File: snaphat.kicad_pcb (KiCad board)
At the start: 2 copper layers, 100 x 65.1 mm, 111 parts, among them J1 Conn_01x08_S8B-PH-K-S(LF)(SN), J2 Conn_02x20_2214SM-40G-75-PCR, J3 Conn_01x02_B2B-PH-K-S(LF)(SN), J4 USB_C_USB4125-GF-A-0190, J5 Conn_01x03_MC34747, Q1 Q_BC817-25, Q2 Q_NTR4003NT1G, Q3 Q_NTR4003NT1G, SW1 SW_B3FS-1050, SW2 SW_B3FS-1050, SW3 SW_B3FS-1050, SW4 SW_B3FS-1050, SW5 SW_B3FS-1050, SW6 SW_B3FS-1050, SW7 SW_B3FS-1050, SW8 SW_B3F-3150, U1 INA219BIDR, U2 MPQ3414BGJ-5-AEC1-P, U3 MCP73871T-2CCI/ML, U4 1825232-1, U5 AP9101CAK6-ABTRG1, U6 LIS2DW12TR

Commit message: Start updating PCB, library fixes
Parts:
- removed C4: 10u, library:C_0805_2012Metric
- removed C5: 1u, library:C_0805_2012Metric
- removed Q3: Q_NTR4003NT1G, library:SOT-23
- removed R17, R19: 0R, library:R_0402_1005Metric
- removed R2: 10k, library:R_0402_1005Metric
- removed REF** (x8): , library:TestPoint_Ornament
- removed REF** (x4): MountingHole_2.7mm, library:MountingHole_2.7mm
- added C10: 10u, library:C_0805_2012Metric, F.Cu at (239.9, 114.5)
- added D6: SL04-E3-08, library:DO-219AB, F.Cu at (231.7, 111.4)
- added D7: SL04-E3-08, library:DO-219AB, F.Cu at (216.7, 114.6)
- added D8: D_SMBJ5.0A, library:D_SMB, F.Cu at (225.4, 130.5)
- added H34: 9774020951R, library:Mounting_Wuerth_WA-SMST-2.7mm_H2mm_9774020951, F.Cu at (175.5, 21.7)
- added H35: 9774020951R, library:Mounting_Wuerth_WA-SMST-2.7mm_H2mm_9774020951, F.Cu at (175.5, 29.2)
- added H36: 9774020951R, library:Mounting_Wuerth_WA-SMST-2.7mm_H2mm_9774020951, F.Cu at (175.5, 36.8)
- added H37: 9774020951R, library:Mounting_Wuerth_WA-SMST-2.7mm_H2mm_9774020951, F.Cu at (175.5, 44.3)
- added J10: P70-6000045R, library:HARWIN_P70-6000045R, F.Cu at (190.9, 25.5)
- added J11: P70-6000045R, library:HARWIN_P70-6000045R, F.Cu at (190.9, 28.6)
- added J12: P70-6000045R, library:HARWIN_P70-6000045R, F.Cu at (190.9, 31.6)
- added J6: Conn_01x04_SFV4R-3STBE1HLF/C, library:AMPHENOL_SFV4R-3STBE1HLF, B.Cu at (193.1, 121.8)
- added J7: Conn_01x04_SFV4R-3STBE1HLF/C, library:AMPHENOL_SFV4R-3STBE1HLF, B.Cu at (175.5, 21.4)
- added J8: P70-6000045R, library:HARWIN_P70-6000045R, F.Cu at (190.9, 19.4)
- added J9: P70-6000045R, library:HARWIN_P70-6000045R, F.Cu at (190.9, 22.5)
- added R28: 330R, library:R_0402_1005Metric, F.Cu at (188.0, 38.9)
- added SW9: 1825232-1, library:1825232-1, B.Cu at (244.2, 113.4)
- C3: value 22u -> 2u2
- D2: value 0805 G LED -> 0805 B LED
- D4: value 0805 B LED -> 0805 R LED
- H15: value 803040 -> 10304
- H26, H27, H28, H29: value 9774030633R -> 9774030151R; footprint library:Mounting_Wuerth_WA-SMSI-M1.6_H3mm_9774030633 -> library:Mounting_Wuerth_WA-SMSI-M2.5_H3mm_9774030151R
- H30, H31, H32: value 970110151 -> 9774100151R; footprint library:970110151 -> library:Mounting_Wuerth_WA-SMSI-M2.5_H10mm_9774100151R
- J4: value USB_C_USB4125-GF-A-0190 -> USB_C_USB4930-00-A; footprint library:USB_C_Receptacle_GCT_USB4125-xx-x-0190_6P_TopMnt_Horizontal -> library:USB_C_Receptacle_GCT_USB4105-xx-A_16P_TopMnt_Horizontal
- L1: value L_SRP3212A-R68M -> L_LQH44PH100MPRL; footprint library:L_1210_3225Metric -> library:L_LPH44PH
- Q2: value Q_NTR4003NT1G -> Q_FDC6561AN; footprint library:SOT-23 -> library:SSOT-6
- R10: value 150R -> 47R
- R14: value 10k -> 2k7
- R6: value 10k -> 100k
- R7: value 10k -> 33k
- R9: value 150R -> 100R
- U2: value MPQ3414BGJ-5-AEC1-P -> MIC2250-1YD5-TR; footprint library:TSOT-23-8 -> library:TSOT-23-5
- U4: value 1825232-1 -> TPD2EUSB30DRTR; footprint library:1825232-1 -> library:Texas_DRT-3
- moved U4 28.4 mm to (216.2, 117.2), turned to 0 degrees
- moved TP11 21.6 mm to (257.3, 103.9)
- moved C2 13.3 mm to (214.1, 129.4)
- moved C15 12.6 mm to (211.5, 129.3)
- moved R4 9.79 mm to (219.2, 129.8), turned to 90 degrees
- moved R5 9.17 mm to (217.9, 129.8), turned to 90 degrees
- moved L1 6.25 mm to (235.4, 109.4), turned to 180 degrees
- moved C13 5.80 mm to (229.9, 110.3), turned to 90 degrees
- moved C3 5.78 mm to (228.2, 110.8), turned to -90 degrees
- moved TP8 4.62 mm to (240.1, 110.4), turned to 180 degrees
- moved R20 4.38 mm to (237.7, 122.6), turned to 180 degrees
- moved R23 3.25 mm to (239.7, 120.8)
- moved C14 3.10 mm to (238.2, 113.7), turned to 90 degrees
- moved R13 2.57 mm to (219.9, 111.4), turned to -90 degrees
- moved C21 2.11 mm to (221.0, 111.4)
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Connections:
- net +BATT renamed VBAT
- net ACCEL_INT1 renamed /ACCEL_INT1
- net ACCEL_INT2 renamed /ACCEL_INT2
- net BTN_BACK renamed /BTN_B
- net BTN_MENU renamed /BTN_MENU
- net BTN_OK renamed /BTN_A
- net CHARGING_STAT renamed /Power supply/CHRG_DONE_STAT
- net I2C_SCL renamed /I2C_SCL
- net I2C_SDA renamed /I2C_SDA
- net Net-(J3-Pin_1) renamed /Power supply/BATTERY_P
- net PROG1 renamed /Power supply/PROG1
- net PROG2 renamed /Power supply/PROG2
- net TIMER_EN renamed Net-(U3-~{TE})
- C15 pad 2: VBUS -> /USBC_VBUS_IN
- C17 pad 2: Net-(C17-Pad2) -> /Power supply/VOUT
- C2 pad 1: VBUS -> /USBC_VBUS_IN
- D3 pad 2: VBUS -> /LOW_BATTERY
- J1 pad 2: GND -> +5V
- J1 pad 5: DISPLAY_SPI_CS -> +5V
- J1 pad 6: DISPLAY_DC -> +5V
- J1 pad 7: DISPLAY_RST -> +5V
- J1 pad 8: DISPLAY_BL -> +5V
- J2 pad 10: RPI_UART_RX -> GND
- J2 pad 12: BUZZER_SIGNAL -> GND
- J2 pad 18: DISPLAY_RST -> GND
- J2 pad 19: DISPLAY_SPI_MOSI -> /DISPLAY_MOSI
- J2 pad 22: DISPLAY_DC -> GND
- J2 pad 23: DISPLAY_SPI_SCLK -> /DISPLAY_SPI_SCLK
- J2 pad 24: DISPLAY_SPI_CS -> GND
- J2 pad 27: unconnected-(J2-Pin_27-Pad27) -> /BTN_D
- J2 pad 29: BTN_D -> /BTN_L
- J2 pad 31: BTN_L -> /BTN_R
- J2 pad 32: DISPLAY_BL -> GND
- J2 pad 33: BTN_R -> /BTN_U
- J2 pad 35: BTN_U -> /LOW_BATTERY
- J2 pad 37: BTN_SHUTTER -> /BTN_SHUTTER
- J2 pad 8: RPI_UART_TX -> GND
- J4 pad A9: VBUS -> /USBC_VBUS_IN
- J4 pad B9: VBUS -> /USBC_VBUS_IN
- J5 pad 1: RPI_UART_RX -> GND
- J5 pad 2: RPI_UART_TX -> GND
- L1 pad 2: Net-(U2-SW) -> Net-(D6-A)
- Q1 pad 1: Net-(Q1-C) -> Net-(Q1-B)
- Q1 pad 2: Net-(Q1-B) -> GND
- Q1 pad 3: GND -> Net-(BZ1--)
- Q2 pad 1: Net-(Q2-D) -> Net-(U5-DO)
- Q2 pad 2: Net-(Q2-G) -> GND
- Q2 pad 3: GNDS -> Net-(U5-CO)
- R1 pad 1: BUZZER_SIGNAL -> GND
- R10 pad 1: LBO_STAT -> GND
- R14 pad 1: PROG3 -> GND
- R14 pad 2: GND -> /Power supply/PROG3
- R18 pad 1: PS_SELECT -> VBUS
- R18 pad 2: VBUS -> Net-(U3-SEL)
- R27 pad 1: Net-(BZ1--) -> /GND_EXT
- R27 pad 2: Net-(Q1-C) -> /OTG_EXT
- R4 pad 1: Net-(J4-CC2) -> GND
- R4 pad 2: GND -> Net-(J4-CC1)
- R5 pad 1: Net-(J4-CC1) -> GND
- R5 pad 2: GND -> Net-(J4-CC2)
- R6 pad 1: VSYS -> +5V
- R6 pad 2: Net-(U2-MODE) -> Net-(U2-FB)
- R7 pad 1: VSYS -> Net-(U2-FB)
- R7 pad 2: Net-(U2-EN) -> GND
- R8 pad 1: POWER_GOOD -> /Power supply/CHRG_STAT
- SW4 pad 1: BTN_U -> /BTN_U
- SW4 pad 2: BTN_U -> /BTN_U
- SW5 pad 1: BTN_L -> /BTN_L
- SW5 pad 2: BTN_L -> /BTN_L
- SW6 pad 1: BTN_R -> /BTN_R
- SW6 pad 2: BTN_R -> /BTN_R
- SW7 pad 1: BTN_D -> /BTN_D
- SW7 pad 2: BTN_D -> /BTN_D
- SW8 pad 1: BTN_SHUTTER -> /BTN_SHUTTER
- SW8 pad 2: BTN_SHUTTER -> GND
- U2 pad 1: VSYS -> Net-(D6-A)
- U2 pad 2: +5V -> GND
- U2 pad 3: Net-(U2-SW) -> Net-(U2-FB)
- U2 pad 4: GND -> VSYS
- U2 pad 5: GND -> VSYS
- U3 pad 1: Net-(C17-Pad2) -> /Power supply/VOUT
- U3 pad 12: PROG3 -> /Power supply/PROG3
- U3 pad 20: Net-(C17-Pad2) -> /Power supply/VOUT
- U3 pad 3: PS_SELECT -> Net-(U3-SEL)
- U3 pad 6: POWER_GOOD -> unconnected-(U3-~{PG}-Pad6)
- U3 pad 8: LBO_STAT -> /Power supply/CHRG_STAT
- U4 pad 1: Net-(C17-Pad2) -> /USBC_DATA_P
- U4 pad 2: VSYS -> /USBC_DATA_N
- U4 pad 3: unconnected-(U4-Pad3) -> GND
- U5 pad 1: Net-(Q2-G) -> Net-(U5-DO)
- U5 pad 3: Net-(Q3-G) -> Net-(U5-CO)
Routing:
- net +5V: track 113.5 -> 304.9 mm, vias 3 -> 11
- net VBUS: track 112.9 -> 3.99 mm, vias 5 -> 0
- net BTN_R: track 69.7 -> 0.00 mm, vias 1 -> 0
- net /BTN_R: track 0.00 -> 68.3 mm, vias 0 -> 1
- net /LOW_BATTERY: track 0.00 -> 64.3 mm, vias 0 -> 1
- net BTN_D: track 62.8 -> 0.00 mm, vias 1 -> 0
- net BTN_U: track 62.1 -> 0.00 mm, vias 1 -> 0
- net /BTN_D: track 0.00 -> 61.1 mm, vias 0 -> 1
- net /BTN_U: track 0.00 -> 59.1 mm, vias 0 -> 1
- net GND: track 42.0 -> 97.6 mm, vias 22 -> 1
- net BTN_SHUTTER: track 53.8 -> 0.00 mm
- net BTN_L: track 52.5 -> 0.00 mm, vias 1 -> 0
- net /BTN_L: track 0.00 -> 51.9 mm, vias 0 -> 1
- net LBO_STAT: track 51.2 -> 0.00 mm, vias 1 -> 0
- net DISPLAY_RST: track 50.6 -> 0.00 mm
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- added copper zone on B.Cu, net /Power supply/VOUT
- added copper zone on F.Cu, net Net-(D6-A)
- added copper zone on B.Cu, net Net-(Q2-Pad4)
- removed copper zone on B.Cu, net Net-(C17-Pad2)
- removed copper zone on F.Cu, net Net-(U2-SW)

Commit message: Rerouted power and USB
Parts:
- removed U4: TPD2EUSB30DRTR, library:Texas_DRT-3
- added C22: 100n, library:C_0402_1005Metric, B.Cu at (212.8, 120.0)
- added D9: SP1004U-ULC-04UTG, library:SP1004UULC04UTG, B.Cu at (215.7, 119.0)
- added REF**: MountingHole_2.7mm, MountingHole:MountingHole_2.7mm, F.Cu at (243.7, 125.5)
- C15, C2, D7, R11, R4, R5, TP6: moved to B.Cu
- D8: footprint library:D_SMB -> library:SOD-123FL
- moved TP11 23.1 mm to (234.8, 109.4), turned to -90 degrees
- moved TP6 15.8 mm to (228.3, 118.4), turned to 90 degrees
- moved C2 13.2 mm to (222.4, 119.2)
- moved R5 13.1 mm to (214.1, 117.3), turned to 0 degrees
- moved R4 12.6 mm to (217.4, 117.3), turned to 180 degrees
- moved C15 12.3 mm to (219.6, 120.0)
- moved D8 10.3 mm to (216.2, 126.1), turned to -90 degrees
- moved R9 8.07 mm to (222.3, 122.4)
- moved R11 6.71 mm to (229.0, 109.1), turned to 180 degrees
- moved R8 5.46 mm to (223.3, 122.4)
- moved D7 4.00 mm to (220.2, 116.6), turned to -90 degrees
- moved R22 3.74 mm to (239.0, 125.7)
- moved R3 3.20 mm to (235.3, 113.5)
- moved J5 3.13 mm to (170.4, 118.1)
- moved U1 3.04 mm to (234.0, 119.5)
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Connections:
- J1 pad 2: +5V -> GND
- J1 pad 3: DISPLAY_SPI_MOSI -> /DISPLAY_MOSI
- J1 pad 4: DISPLAY_SPI_SCLK -> /DISPLAY_SPI_SCLK
- J1 pad 5: +5V -> GND
- J1 pad 6: +5V -> GND
- J1 pad 7: +5V -> GND
- J1 pad 8: +5V -> GND
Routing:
- net GND: track 97.6 -> 223.6 mm, vias 1 -> 14
- net +5V: track 304.9 -> 183.9 mm, vias 11 -> 7
- net VBUS: track 3.99 -> 55.9 mm, vias 0 -> 7
- net DISPLAY_SPI_MOSI: track 50.3 -> 0.00 mm
- net DISPLAY_SPI_SCLK: track 42.0 -> 0.00 mm
- net /DISPLAY_MOSI: track 0.00 -> 40.6 mm
- net /I2C_SCL: track 61.9 -> 101.6 mm
- net +3.3V: track 147.3 -> 182.3 mm, vias 6 -> 8
- net /DISPLAY_SPI_SCLK: track 0.00 -> 32.5 mm
- net /I2C_SDA: track 72.0 -> 101.5 mm
- net /BTN_B: track 21.3 -> 32.5 mm
- net /Power supply/VOUT: track 48.2 -> 37.9 mm
- net Net-(D2-K): track 1.55 -> 10.7 mm
- net /USBC_VBUS_IN: track 0.00 -> 8.52 mm, vias 0 -> 4
- net /BTN_MENU: track 23.0 -> 31.3 mm
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- added copper zone on B.Cu, net /USBC_VBUS_IN
- added copper zone on F.Cu, net /USBC_VBUS_IN
- removed copper zone on B.Cu, net Net-(Q2-Pad4)
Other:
- board size 100 x 65.1 mm -> 100 x 68.1 mm

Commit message: Fix RPi connector on schematic, route rest of signals
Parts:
- removed REF**: MountingHole_2.7mm, MountingHole:MountingHole_2.7mm
- moved R27 78.6 mm to (187.5, 43.4)
- moved R1 1.99 mm to (159.6, 110.5)
- moved R6 0.84 mm to (234.8, 116.3), turned to 180 degrees
- moved R7 0.71 mm to (234.8, 117.3), turned to 0 degrees
- moved Q1 0.08 mm to (158.2, 113.0), turned to 180 degrees
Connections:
- J1 pad 5: GND -> /DISPLAY_SPI_CS
- J1 pad 6: GND -> /DISPLAY_DC
- J1 pad 7: GND -> /DISPLAY_RST
- J1 pad 8: GND -> /DISPLAY_BL
- J2 pad 10: GND -> /RPI_UART_RX
- J2 pad 12: GND -> /BUZZER_SIGNAL
- J2 pad 18: GND -> /DISPLAY_RST
- J2 pad 22: GND -> /DISPLAY_DC
- J2 pad 24: GND -> /DISPLAY_SPI_CS
- J2 pad 32: GND -> /DISPLAY_BL
- J2 pad 8: GND -> /RPI_UART_TX
- J5 pad 1: GND -> /RPI_UART_RX
- J5 pad 2: GND -> /RPI_UART_TX
- R1 pad 1: GND -> /BUZZER_SIGNAL
- R28 pad 1: GND -> /DISPLAY_BL
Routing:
- net GND: track 223.6 -> 92.6 mm, vias 14 -> 20
- net +5V: track 183.9 -> 121.8 mm, vias 7 -> 3
- net /DISPLAY_RST: track 0.00 -> 49.6 mm
- net /DISPLAY_BL: track 0.00 -> 44.1 mm
- net /DISPLAY_DC: track 0.00 -> 43.4 mm
- net /DISPLAY_SPI_CS: track 0.00 -> 39.3 mm
- net /BUZZER_SIGNAL: track 0.00 -> 24.1 mm
- net /RPI_UART_RX: track 0.00 -> 18.8 mm
- net /RPI_UART_TX: track 0.00 -> 15.1 mm
- net /DISPLAY_SPI_SCLK: track 32.5 -> 42.0 mm
- net /DISPLAY_MOSI: track 40.6 -> 49.8 mm
- net /BTN_B: track 32.5 -> 37.7 mm
- net Net-(BZ1--): track 6.79 -> 8.76 mm
- net /I2C_SCL: track 101.6 -> 102.7 mm
- net Net-(U1-VIN+): track 25.4 -> 24.5 mm
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
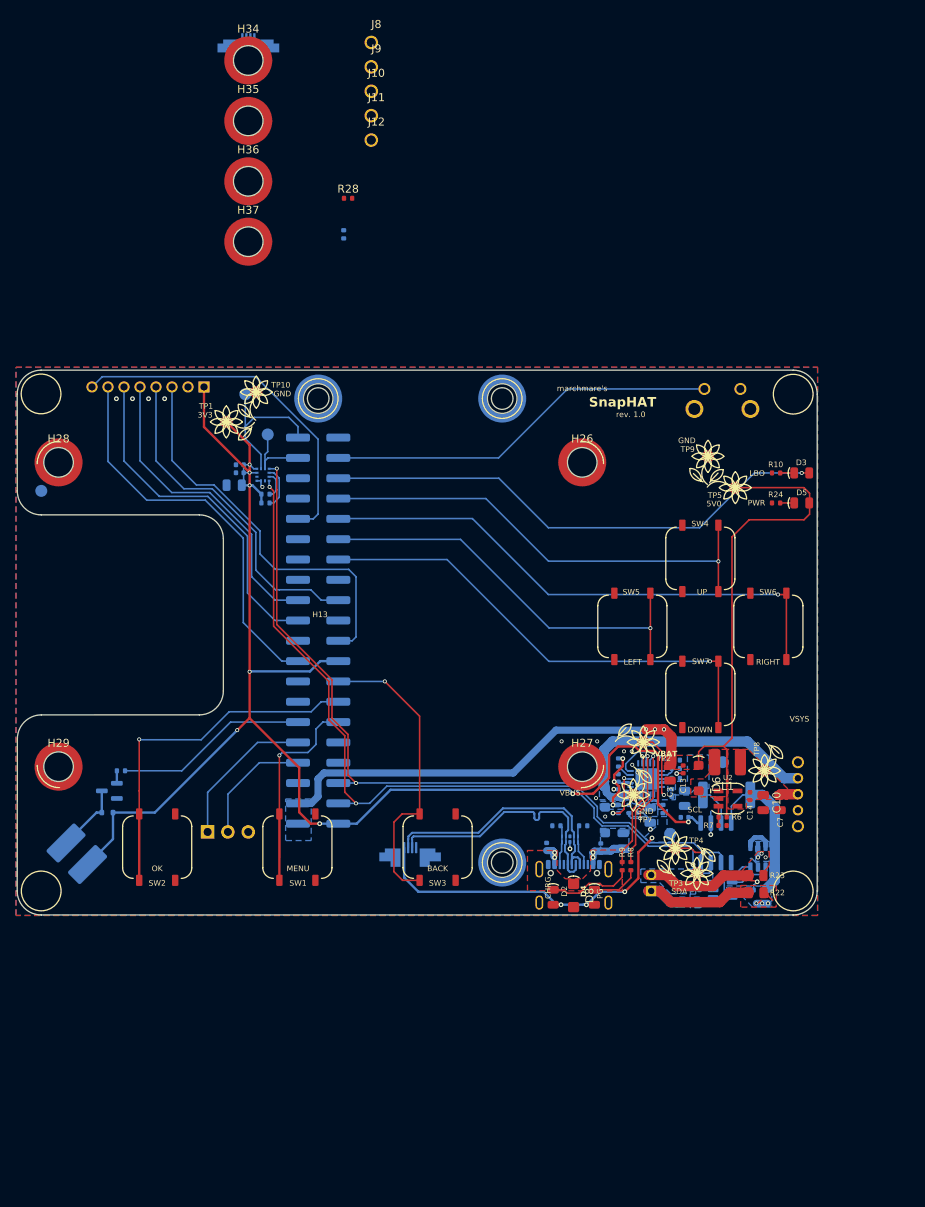
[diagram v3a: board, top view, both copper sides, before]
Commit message: Layout nits, add proper mounting holes
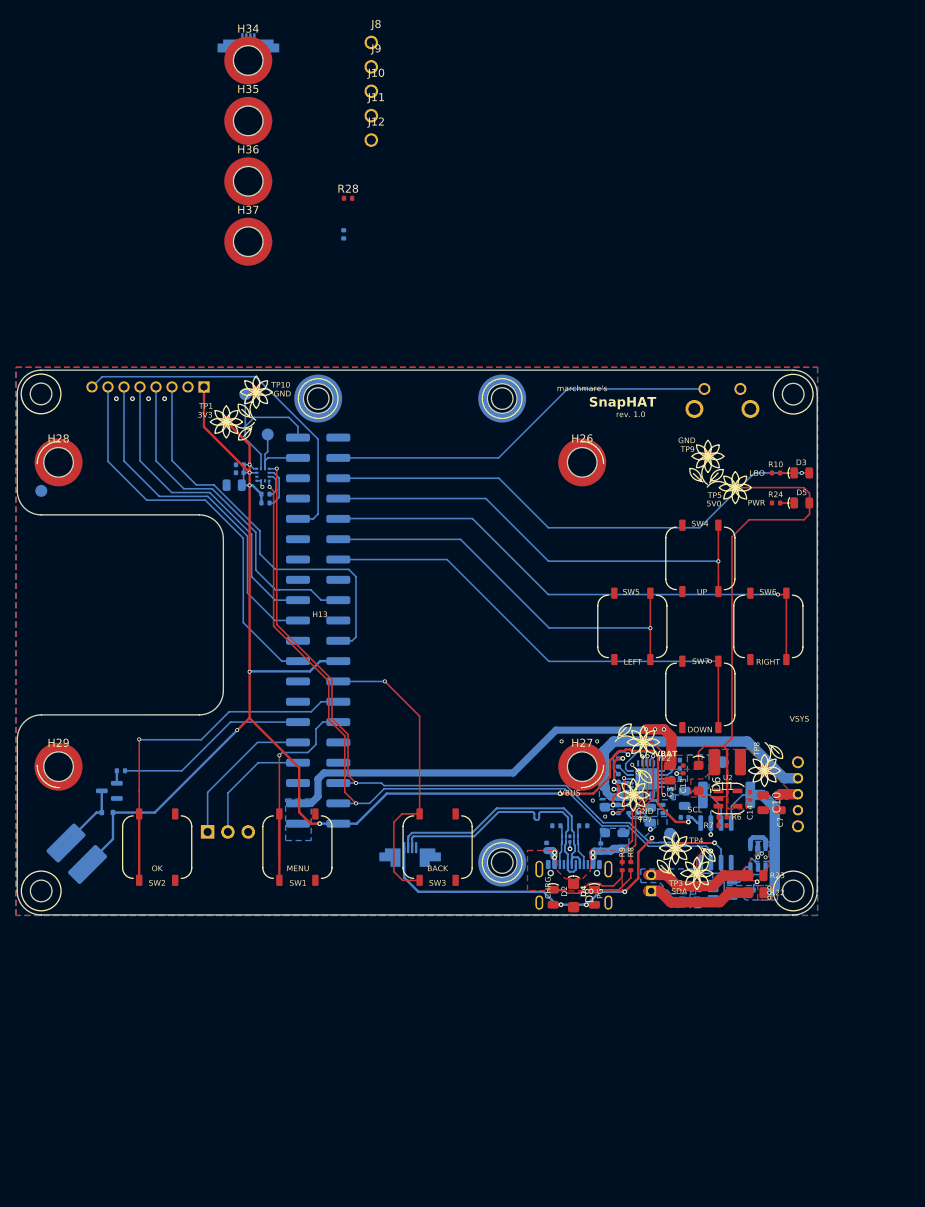
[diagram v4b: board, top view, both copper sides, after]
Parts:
- added H33: MountingHole, library:MountingHole_2.7mm, F.Cu at (149.6, 63.4)
- added H38: MountingHole, library:MountingHole_2.7mm, F.Cu at (149.7, 125.5)
- added H39: MountingHole, library:MountingHole_2.7mm, F.Cu at (243.6, 63.4)
- added H51: MountingHole, library:MountingHole_2.7mm, F.Cu at (243.6, 125.5)
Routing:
- net /I2C_SCL: track 102.7 -> 107.4 mm
- net Net-(U1-VIN+): track 24.5 -> 19.9 mm
- net GND: track 92.6 -> 95.7 mm, vias 20 -> 19
- net +3.3V: track 182.3 -> 181.1 mm

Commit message: Zone fixes
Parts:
- moved TP11 1.37 mm to (233.5, 109.7)
- moved C18 0.66 mm to (224.1, 115.9)
- moved R18 0.65 mm to (221.9, 115.9)
- moved R16 0.64 mm to (223.0, 115.9)
- moved R20 0.61 mm to (237.9, 124.8), turned to -90 degrees
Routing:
- net GND: track 95.7 -> 91.7 mm
- net GNDS: track 15.0 -> 13.7 mm
- net Net-(U3-~{TE}): track 11.4 -> 10.6 mm
- net Net-(U3-SEL): track 7.01 -> 7.73 mm

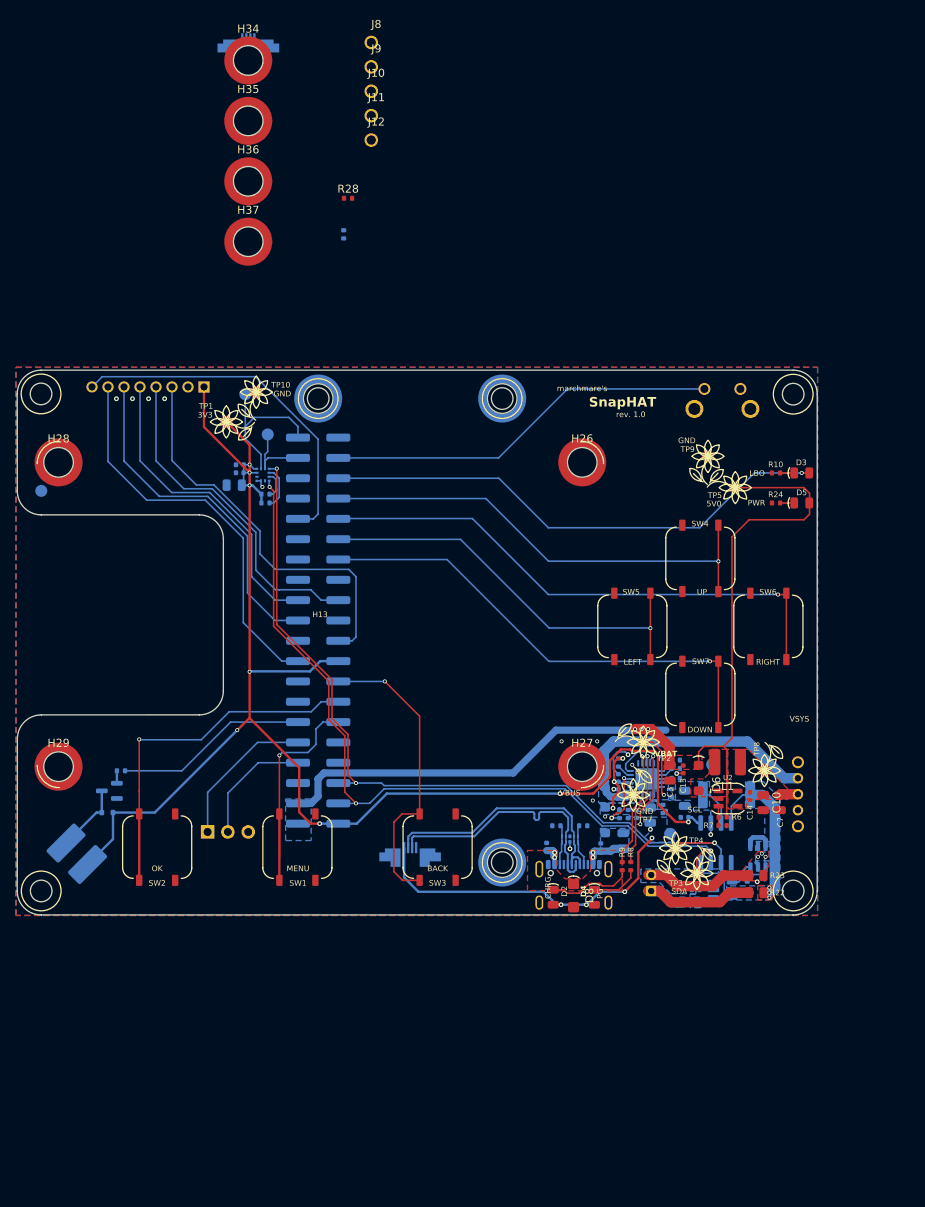
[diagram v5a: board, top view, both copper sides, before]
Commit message: Fix initial DRC problems, add draft USB hat
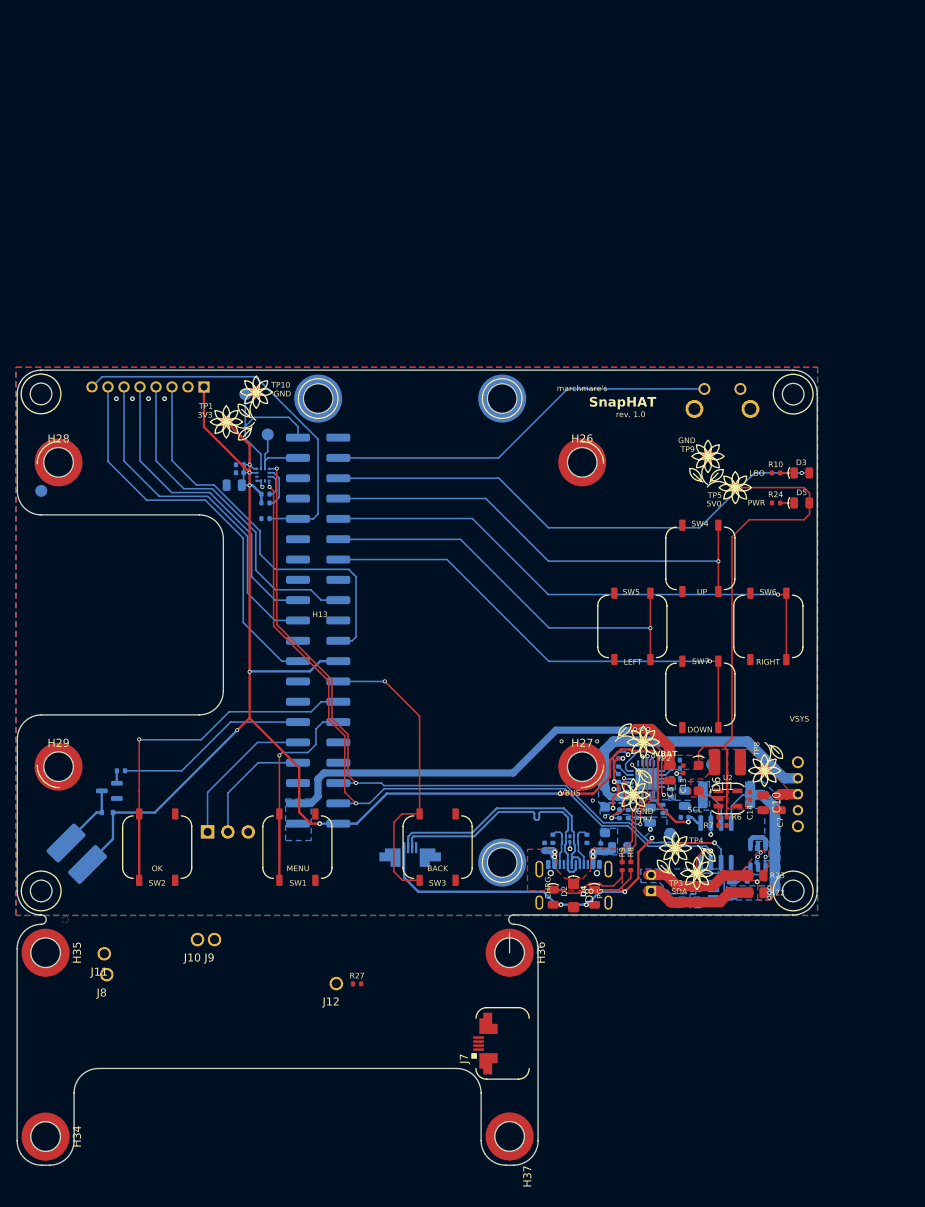
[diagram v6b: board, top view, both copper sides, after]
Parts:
- J7, R27: moved to F.Cu
- R28: moved to B.Cu
- moved H34 136.9 mm to (150.2, 156.2), turned to -90 degrees
- moved J7 127.1 mm to (206.7, 144.6), turned to 90 degrees
- moved J8 121.1 mm to (157.8, 136.0), turned to 180 degrees
- moved H37 116.5 mm to (208.2, 156.2), turned to -90 degrees
- moved J9 110.8 mm to (171.3, 131.6), turned to 180 degrees
- moved J11 109.9 mm to (157.5, 133.3), turned to 180 degrees
- moved J10 108.2 mm to (169.2, 131.6), turned to 180 degrees
- moved H35 107.0 mm to (150.2, 133.2), turned to -90 degrees
- moved J12 105.5 mm to (186.5, 137.1), turned to 180 degrees
- moved H36 101.8 mm to (208.2, 133.2), turned to -90 degrees
- moved R27 93.7 mm to (189.1, 137.1), turned to 180 degrees
- moved R28 41.3 mm to (177.7, 79.0), turned to 180 degrees
- moved R4 1.70 mm to (217.9, 119.0), turned to 90 degrees
- moved R5 1.69 mm to (213.6, 119.0), turned to 90 degrees
- moved C2 0.99 mm to (222.0, 120.1), turned to 0 degrees
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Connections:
- J7 pad 1: /GND_EXT -> /VBUS_EXT
- J7 pad 2: /USBC_EXT_DATA_P -> /USBC_EXT_DATA_N
- J7 pad 3: /USBC_EXT_DATA_N -> /USBC_EXT_DATA_P
- J7 pad 4: /VBUS_EXT -> /GND_EXT
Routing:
- net GND: track 91.7 -> 98.9 mm
- net /DISPLAY_BL: track 44.1 -> 47.7 mm
- net +5V: track 121.9 -> 119.7 mm
- net /USBC_VBUS_IN: track 8.52 -> 6.97 mm
- net Net-(U3-~{TE}): track 10.6 -> 11.9 mm
- net VBUS: track 55.6 -> 56.3 mm
- net (no net): vias 0 -> 1
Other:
- board size 100 x 68.1 mm -> 100 x 99.4 mm
